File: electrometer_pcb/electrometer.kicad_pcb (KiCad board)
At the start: 2 copper layers, 50 x 50 mm, 27 parts, among them J2 Conn_01x03_Pin, J3 Screw_Terminal_01x03, J4 PRT-14417, U1 LMC6082, U2 ADS1115IDGS, U3 REF3025, U4 5V LDO, U5 INA159AIDGKR

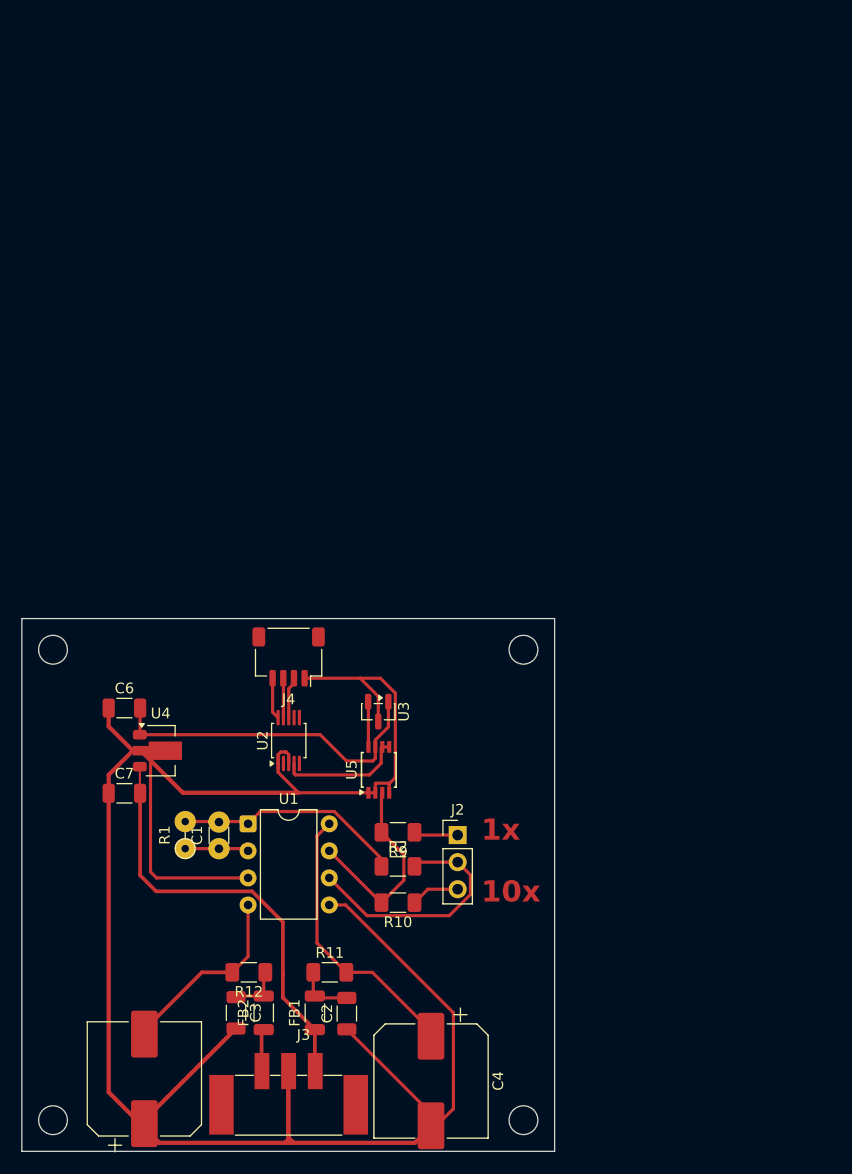
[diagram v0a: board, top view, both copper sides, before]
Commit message: committing before pull. changed size of electrometer board
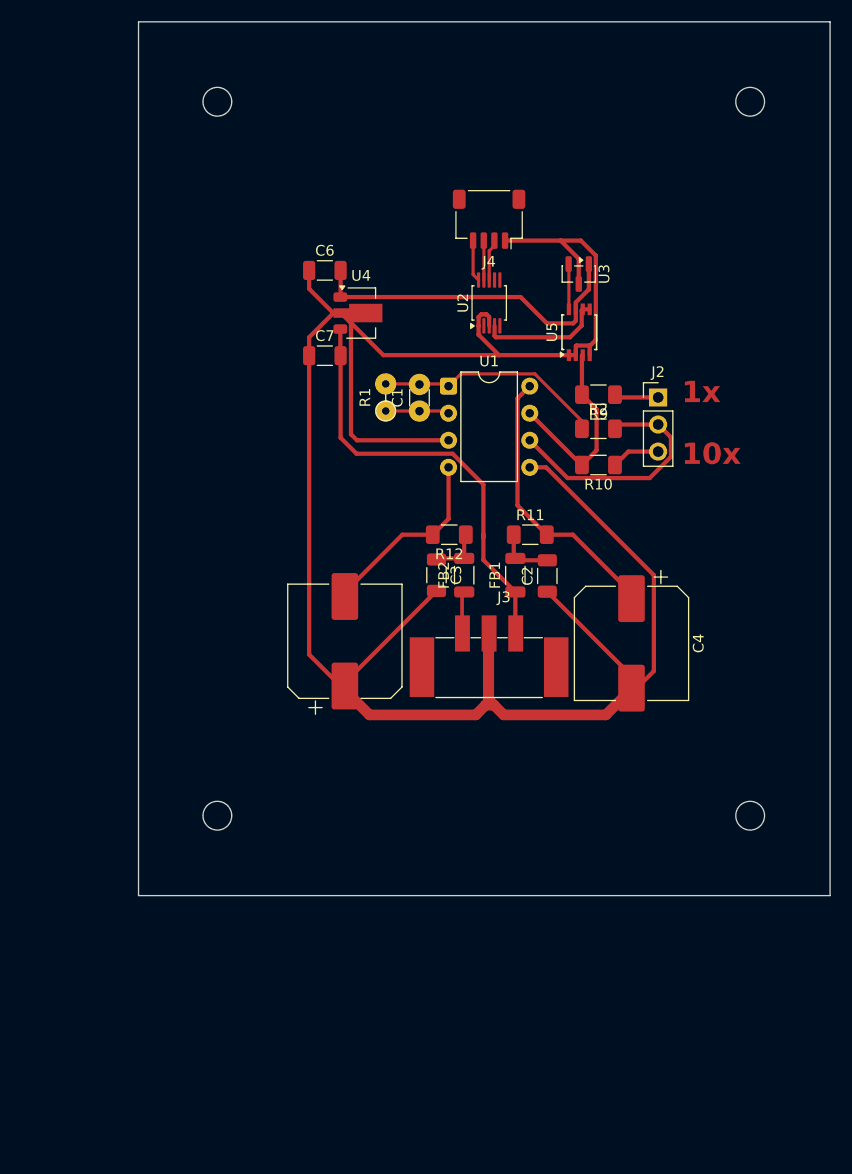
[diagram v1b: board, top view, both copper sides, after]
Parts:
- removed the REF** at (79.0, 142.1)
- removed the REF** at (123.2, 142.1)
- removed the REF** at (123.2, 97.9)
- removed the REF** at (79.0, 97.9)
- added REF**: MountingHole_2.7mm, MountingHole:MountingHole_2.7mm, F.Cu at (94.5, 113.5)
- added REF**: MountingHole_2.7mm, MountingHole:MountingHole_2.7mm, F.Cu at (144.5, 46.5)
- added REF**: MountingHole_2.7mm, MountingHole:MountingHole_2.7mm, F.Cu at (94.5, 46.5)
- added REF**: MountingHole_2.7mm, MountingHole:MountingHole_2.7mm, F.Cu at (144.5, 113.5)
- moved C3 45.2 mm to (115.0, 90.9)
- moved C4 45.2 mm to (133.3, 97.3)
- moved C6 45.2 mm to (104.5, 62.3)
- moved C7 45.2 mm to (104.5, 70.3)
- moved FB1 45.2 mm to (122.4, 90.9)
- moved FB2 45.2 mm to (117.6, 90.9)
- moved R1 45.2 mm to (110.2, 75.5)
- moved R2 45.2 mm to (130.2, 77.2)
- moved R9 45.2 mm to (130.2, 74.0)
- moved U1 45.2 mm to (116.1, 73.2)
- moved U2 45.2 mm to (120.0, 65.4)
- moved U4 45.2 mm to (107.9, 66.3)
- moved U5 45.2 mm to (128.4, 68.1)
- moved C1 45.2 mm to (113.4, 75.5)
- moved C2 45.2 mm to (125.4, 91.0)
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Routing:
- net GND: track 215.6 -> 217.2 mm
- net /Output: track 19.0 -> 18.4 mm
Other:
- board size 50 x 50 mm -> 64.9 x 82 mm
